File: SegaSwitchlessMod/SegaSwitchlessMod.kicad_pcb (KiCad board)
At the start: 2 copper layers, 34 x 29.7 mm, 13 parts, among them J10 JP10, J12 JP12, J6 JP6, U4 PIC16F630-IP

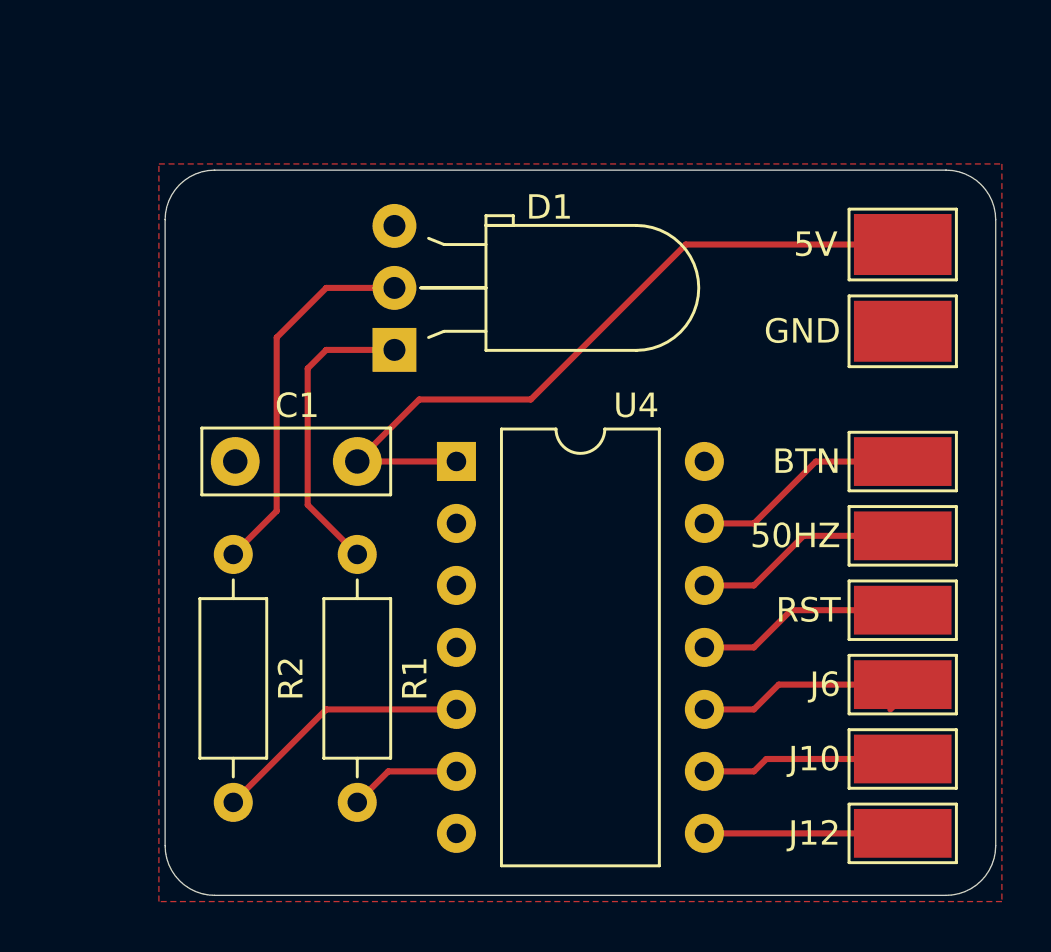
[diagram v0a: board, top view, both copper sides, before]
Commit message: re-layout sega mod to fit Mega Drive II better
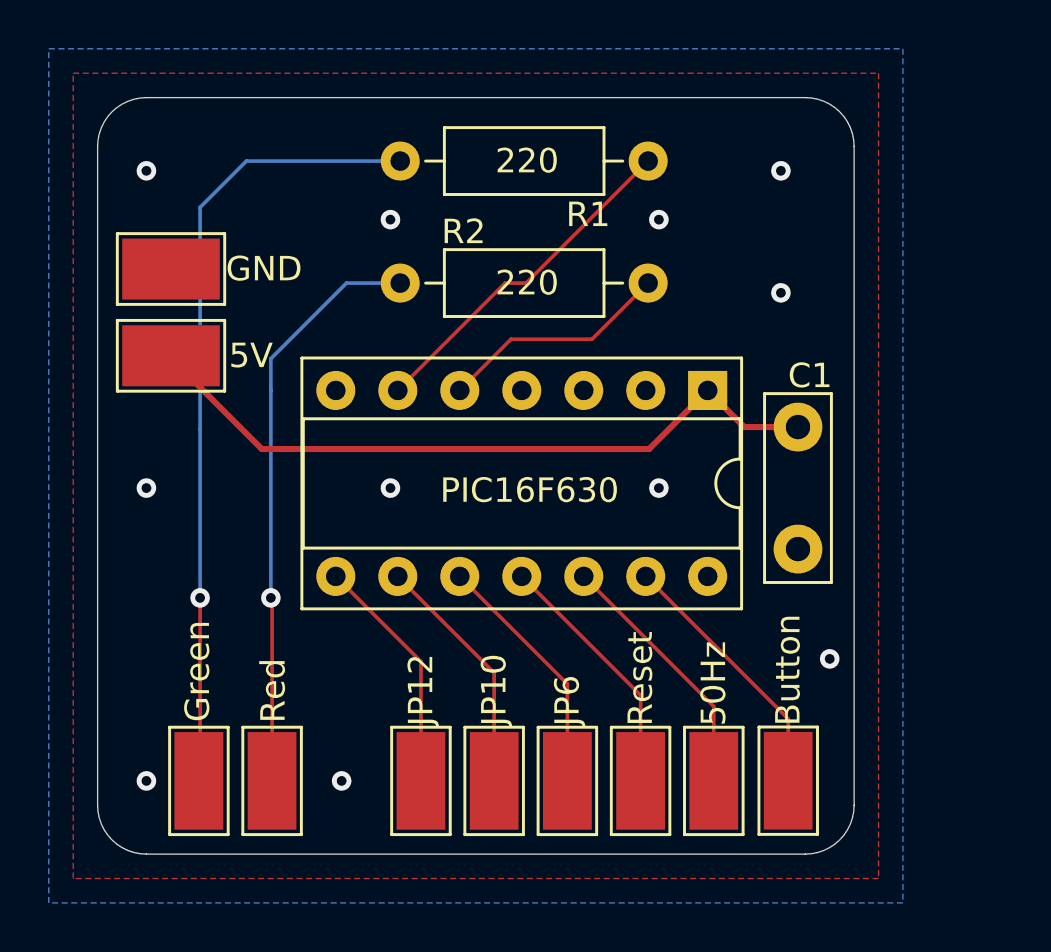
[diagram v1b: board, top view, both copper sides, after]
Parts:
- removed 50HZ: 50, SegaSwitchlessMod:WireSolderPad_2.0x4.0mm
- removed D1: LED_Dual_AAC, LED_THT:LED_D5.0mm-3_Horizontal_O3.81mm_Z3.0mm
- added 50Hz: 50, SegaSwitchlessMod:WireSolderPad_2.0x4.0mm, F.Cu at (55.0, 55.0)
- added Green: Green, SegaSwitchlessMod:WireSolderPad_2.0x4.0mm, F.Cu at (34.4, 55.0)
- added Red: Red, SegaSwitchlessMod:WireSolderPad_2.0x4.0mm, F.Cu at (37.4, 55.0)
- U4: footprint Package_DIP:DIP-14_W10.16mm -> Package_DIP:DIP-14_W7.62mm_Socket
- moved 5V 30.3 mm to (33.0, 37.6), turned to 180 degrees
- moved GND 30.1 mm to (33.0, 34.0), turned to 0 degrees
- moved C1 23.3 mm to (58.7, 45.5), turned to 90 degrees
- moved JP12 20.1 mm to (43.0, 55.0), turned to 270 degrees
- moved JP10 17.0 mm to (46.0, 55.0), turned to 270 degrees
- moved R1 16.2 mm to (42.4, 29.6), turned to 0 degrees
- moved JP6 14.5 mm to (49.0, 55.0), turned to 270 degrees
- moved Button 13.7 mm to (58.0, 55.0), turned to 270 degrees
- moved R2 13.1 mm to (42.4, 34.6), turned to 0 degrees
- moved Reset 12.9 mm to (52.0, 55.0), turned to 270 degrees
- moved U4 10.7 mm to (55.0, 39.0), turned to 270 degrees
- renumbered BTN to Button, J10 to JP10, J12 to JP12, J6 to JP6, RST to Reset
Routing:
- net Net-(R1-Pad1): track 12.3 -> 32.5 mm, vias 0 -> 1
- net Net-(R1-Pad2): track 4.84 -> 14.2 mm
- net Net-(R2-Pad1): track 15.3 -> 23.9 mm, vias 0 -> 1
- net Net-(U4-Pad8): track 8.13 -> 9.83 mm
- net Net-(U4-Pad9): track 8.34 -> 10.0 mm
- net Net-(U3-Pad1): track 8.76 -> 10.4 mm
- net Net-(U2-Pad1): track 8.97 -> 10.6 mm
- net Net-(U1-Pad1): track 9.18 -> 10.8 mm
- net Net-(R2-Pad2): track 10.7 -> 9.54 mm
- net +5V: track 30.1 -> 29.0 mm
- net Net-(U4-Pad10): track 9.27 -> 10.2 mm
- net GND: vias 0 -> 11
- added copper zone on B.Cu, net GND
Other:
- board size 34 x 29.7 mm -> 31 x 31 mm
- net class 5V added: clearance 0.15, trace_width 0.25, via_dia 0.8, via_drill 0.4
- net class Default: clearance 0.15 -> 0.1; trace_width 0.25 -> 0.15
- rule trace_clearance: 0.15 -> 0.1
- rule trace_min: 0.127 -> 0.1
- rule via_min_size: 0.4 -> 0.2
- board text added: "100nF"
- board text added: "220"
- board text added: "C1"
- board text added: "PIC16F630"
- board text added: "Switchless Mod rev02 xrstf.de (CC BY-SA 4.0)"
- board text removed: "Sega Switchless Mod v01 based on KNZL's Mod © xrstf.de 2020"
